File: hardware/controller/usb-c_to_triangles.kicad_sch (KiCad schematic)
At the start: 14 parts, among them J1 USB_C_Receptacle_USB2.0_16P, J2 USB_C_Receptacle_USB2.0_16P, U1 SN74LVC1T45DBV, U2 SN74LVC1T45DBV

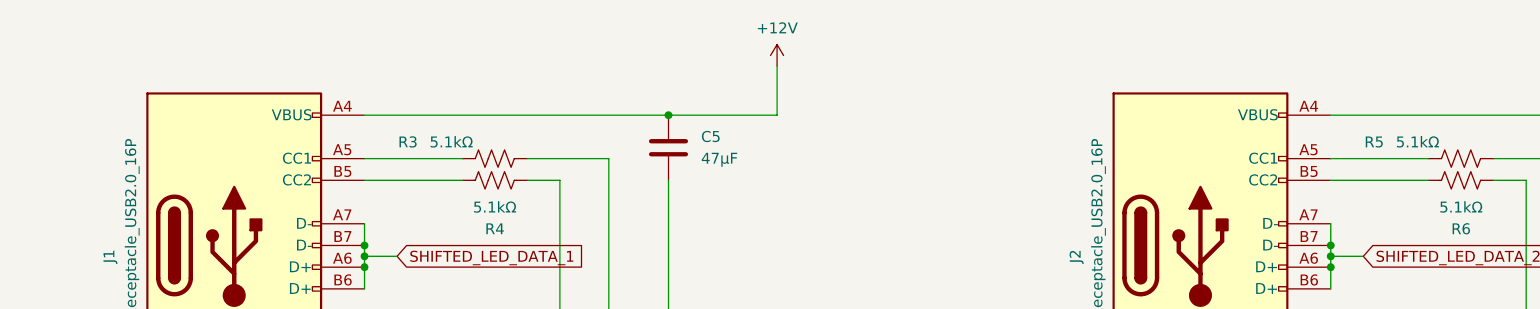
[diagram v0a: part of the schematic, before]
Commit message: adding labels and the barrel connector
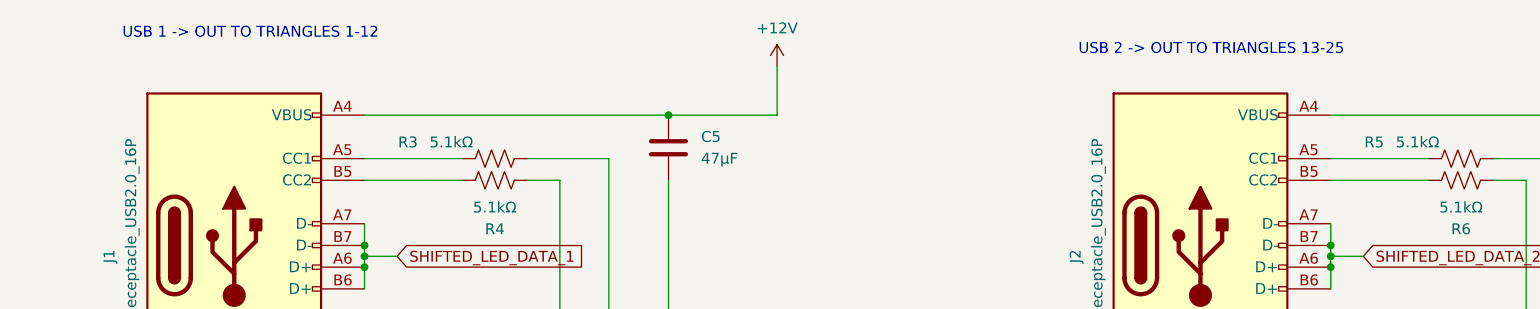
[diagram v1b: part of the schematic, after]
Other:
- note added: "USB 1 -> OUT TO TRIANGLES 1-12"
- note added: "USB 2 -> OUT TO TRIANGLES 13-25"
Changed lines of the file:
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@@
 	(generator_version "10.0")
 	(paper "A4")
+	(text "USB 2 -> OUT TO TRIANGLES 13-25"
+		(exclude_from_sim no)
+		(at 163.83 40.64 0)
+		(effects
+			(font
+				(size 1.27 1.27)
+			)
+		)
+	)
+	(text "USB 1 -> OUT TO TRIANGLES 1-12"
+		(exclude_from_sim no)
+		(at 51.435 38.735 0)
+		(effects
+			(font
+				(size 1.27 1.27)
+			)
+		)
+	)
 	(text "LEVEL SHIFTER 1"
 		(exclude_from_sim no)

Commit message: hook up all the dabao headers and one more voltage converter
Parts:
- C5, C8: footprint Capacitor_SMD:C_1206_3216Metric -> Capacitor_SMD:C_1210_3225Metric
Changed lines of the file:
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@@
 			)
 		)
-		(property "Footprint" "Capacitor_SMD:C_1206_3216Metric"
+		(property "Footprint" "Capacitor_SMD:C_1210_3225Metric"
 			(at 99.3648 48.26 0)
 			(hide yes)
@@
 			)
 		)
-		(property "Footprint" "Capacitor_SMD:C_1206_3216Metric"
+		(property "Footprint" "Capacitor_SMD:C_1210_3225Metric"
 			(at 212.3948 48.26 0)
 			(hide yes)

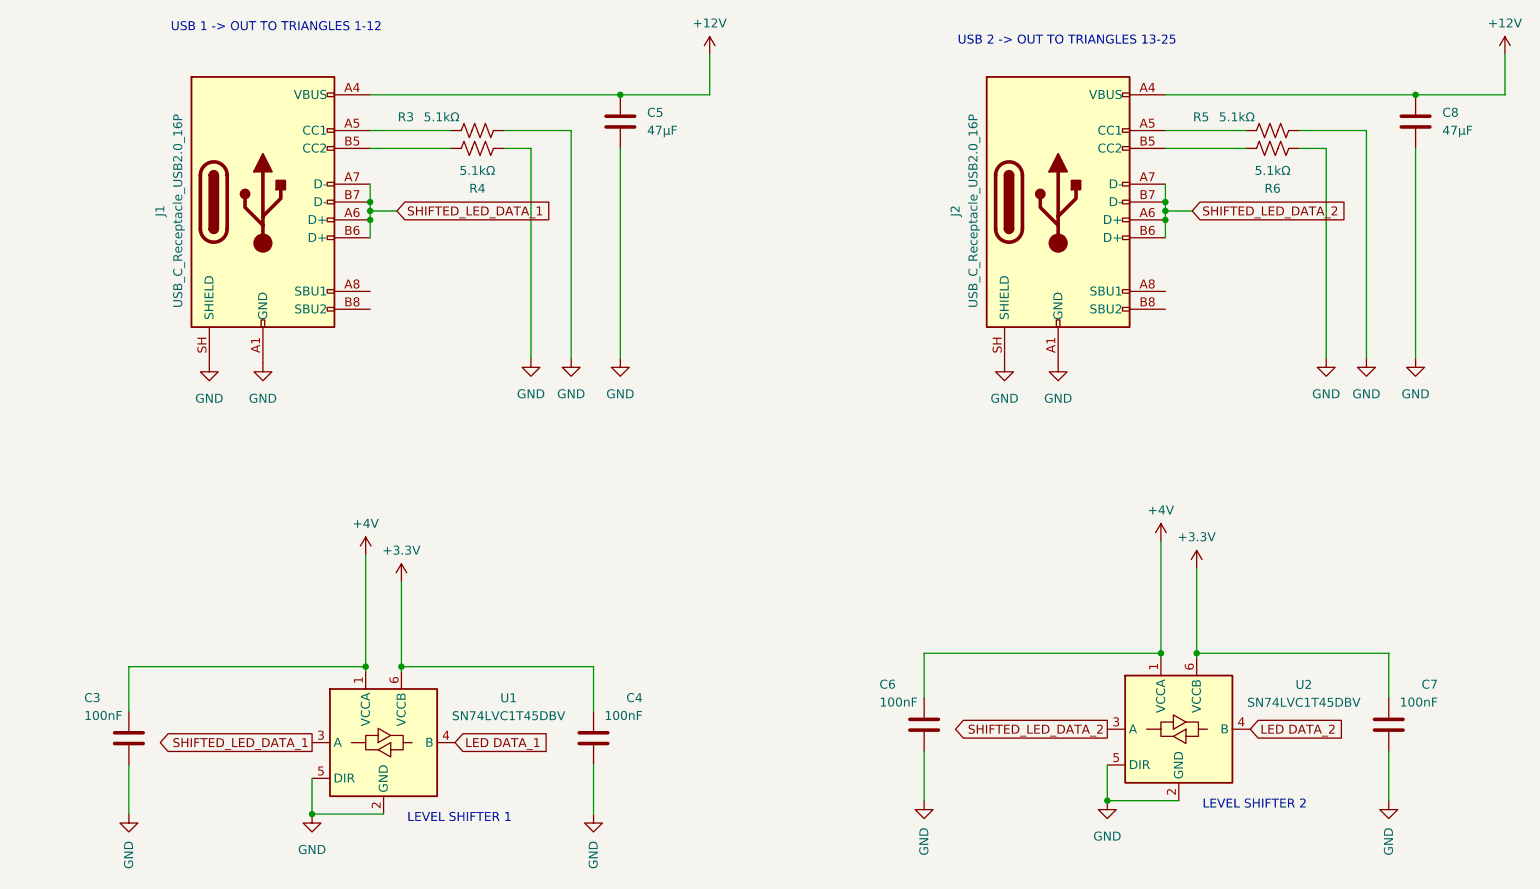
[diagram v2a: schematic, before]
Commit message: re-order the numbers on the schematic for tidiness
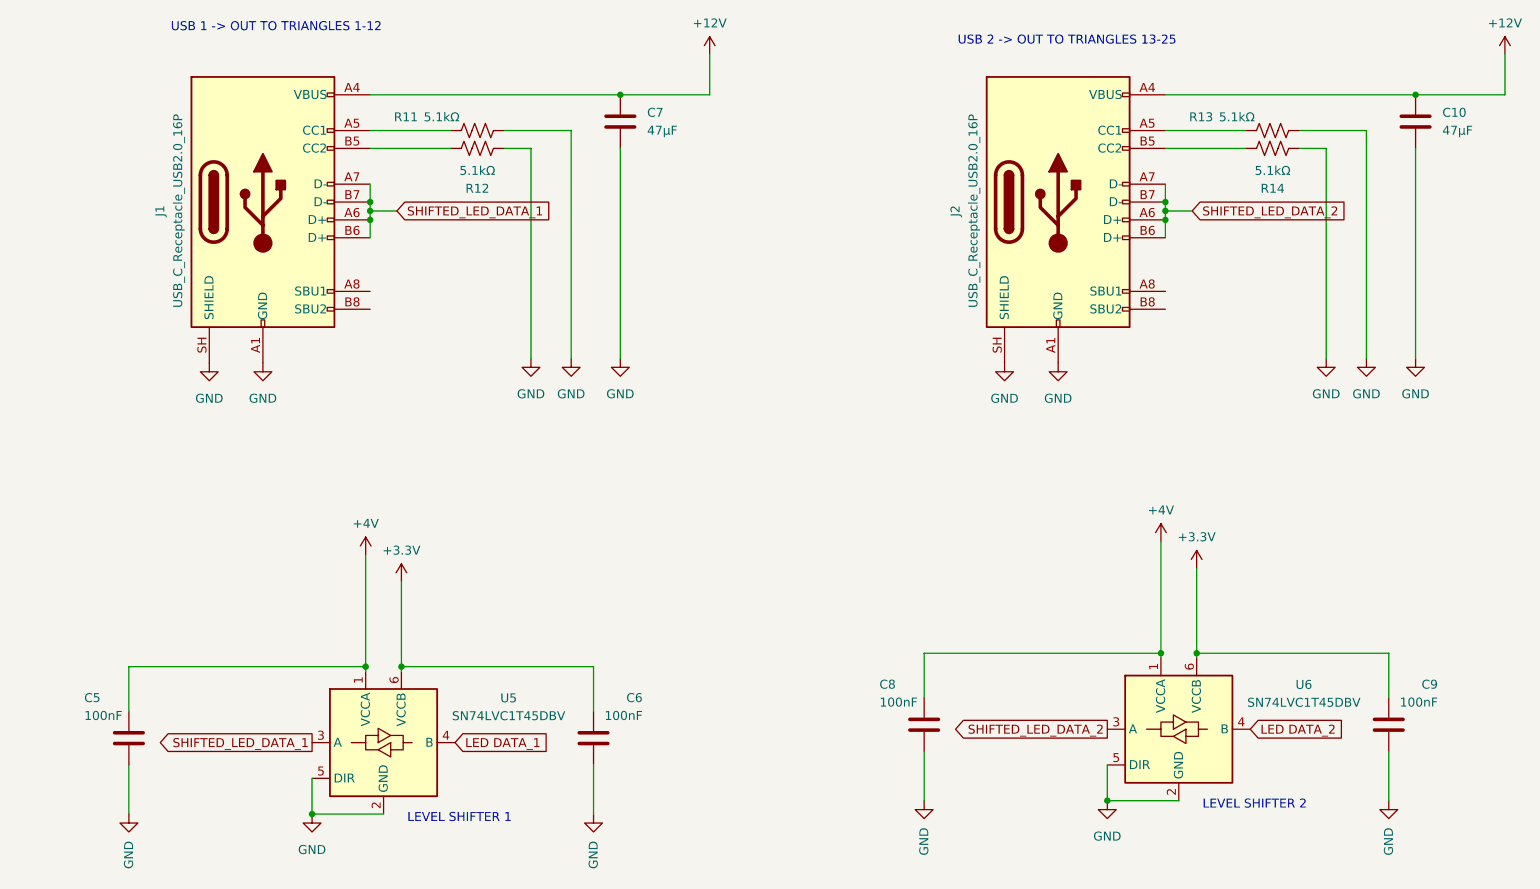
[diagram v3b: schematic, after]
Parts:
- renumbered C8 to C10, C3 to C5, C4 to C6, C5 to C7, C6 to C8, C7 to C9, R3 to R11, R4 to R12, R5 to R13, R6 to R14, U1 to U5, U2 to U6

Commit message: renaming parts for consistency
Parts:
- C10, C7: JLCPCB Part # C77101 -> (none); LCSC Part # (none) -> C77101
- C5, C6, C8, C9: JLCPCB Part # C1525 -> (none); LCSC Part # (none) -> C1525
- J1, J2: JLCPCB # C3151749 -> (none); LCSC Part # (none) -> C3151749
- R11, R12, R13, R14: JLCPCB Part # C23186 -> (none); LCSC Part # (none) -> C23186
- U5, U6: JLCPCB Part # C7843 -> (none); LCSC Part # (none) -> C7843
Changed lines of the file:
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@@
 			)
 		)
-		(property "LCSC Part Number" ""
-			(at 30.48 139.7 0)
-			(hide yes)
-			(show_name no)
-			(do_not_autoplace no)
-			(effects
-				(font
-					(size 1.27 1.27)
-				)
-			)
-		)
-		(property "JLCPCB Part #" "C1525"
+		(property "LCSC Part #" "C1525"
 			(at 30.48 139.7 0)
 			(hide yes)
@@
 			)
 		)
-		(property "JLCPCB Part #" "C23186"
+		(property "LCSC Part #" "C23186"
 			(at 193.04 55.88 90)
 			(hide yes)
@@
 			)
 		)
-		(property "LCSC Part Number" ""
-			(at 143.51 137.795 0)
-			(hide yes)
-			(show_name no)
-			(do_not_autoplace no)
-			(effects
-				(font
-					(size 1.27 1.27)
-				)
-			)
-		)
-		(property "JLCPCB Part #" "C1525"
+		(property "LCSC Part #" "C1525"
 			(at 143.51 137.795 0)
 			(hide yes)
@@
 			)
 		)
-		(property "JLCPCB Part #" "C23186"
+		(property "LCSC Part #" "C23186"
 			(at 80.01 55.88 90)
 			(hide yes)
@@
 			)
 		)
-		(property "JLCPCB Part #" "C23186"
+		(property "LCSC Part #" "C23186"
 			(at 80.01 53.34 90)
 			(hide yes)
@@
 			)
 		)
-		(property "LCSC Part Number" ""
-			(at 209.55 137.795 0)
-			(hide yes)
-			(show_name no)
-			(do_not_autoplace no)
-			(effects
-				(font
-					(size 1.27 1.27)
-				)
-			)
-		)
-		(property "JLCPCB Part #" "C1525"
+		(property "LCSC Part #" "C1525"
 			(at 209.55 137.795 0)
 			(hide yes)
@@
 			)
 		)
-		(property "JLCPCB Part #" "C7843"
+		(property "LCSC Part #" "C7843"
 			(at 66.675 140.335 0)
 			(hide yes)
@@
 			)
 		)
-		(property "JLCPCB Part #" "C77101"
+		(property "LCSC Part #" "C77101"
 			(at 100.33 52.07 0)
 			(hide yes)
@@
 			)
 		)
-		(property "LCSC Part Number" ""
-			(at 96.52 139.7 0)
-			(hide yes)
-			(show_name no)
-			(do_not_autoplace no)
-			(effects
-				(font
-					(size 1.27 1.27)
-				)
-			)
-		)
-		(property "JLCPCB Part #" "C1525"
+		(property "LCSC Part #" "C1525"
 			(at 96.52 139.7 0)
 			(hide yes)
@@
 			)
 		)
-		(property "JLCPCB Part #" "C23186"
+		(property "LCSC Part #" "C23186"
 			(at 193.04 53.34 90)
 			(hide yes)
@@
 			)
 		)
-		(property "JLCPCB #" "C3151749"
+		(property "LCSC Part #" "C3151749"
 			(at 162.56 63.5 90)
 			(hide yes)
@@
 			)
 		)
-		(property "JLCPCB Part #" "C77101"
+		(property "LCSC Part #" "C77101"
 			(at 213.36 52.07 0)
 			(hide yes)
@@
 			)
 		)
-		(property "JLCPCB Part #" "C7843"
+		(property "LCSC Part #" "C7843"
 			(at 179.705 138.43 0)
 			(hide yes)
@@
 			)
 		)
-		(property "JLCPCB #" "C3151749"
+		(property "LCSC Part #" "C3151749"
 			(at 49.53 63.5 90)
 			(hide yes)

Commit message: more footprint updating
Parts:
- J1, J2: footprint footprints:TYPE-C-SMD_USB4120-03-C -> easyeda2kicad:TYPE-C-SMD_USB4120-03-C
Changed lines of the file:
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@@
 			)
 		)
-		(property "Footprint" "footprints:TYPE-C-SMD_USB4120-03-C"
+		(property "Footprint" "easyeda2kicad:TYPE-C-SMD_USB4120-03-C"
 			(at 166.37 63.5 0)
 			(hide yes)
@@
 			)
 		)
-		(property "Footprint" "footprints:TYPE-C-SMD_USB4120-03-C"
+		(property "Footprint" "easyeda2kicad:TYPE-C-SMD_USB4120-03-C"
 			(at 53.34 63.5 0)
 			(hide yes)

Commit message: updating symbols and board
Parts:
- removed J2: USB_C_Receptacle_USB2.0_16P, easyeda2kicad:TYPE-C-SMD_USB4120-03-C, symbol Connector:USB_C_Receptacle_USB2.0_16P
- added J2: TYPE-C 16PLT-H10.0, easyeda2kicad:TYPE-C-SMD_USB4120-03-C, symbol easyeda2kicad:TYPE-C16PLT-H10.0
- J1: value USB_C_Receptacle_USB2.0_16P -> TYPE-C 16PLT-H10.0; symbol Connector:USB_C_Receptacle_USB2.0_16P -> easyeda2kicad:TYPE-C16PLT-H10.0
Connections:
- net +12V: now also J2.A4 (VBUS), J2.A9 (VBUS), J2.B4 (VBUS), J2.B9 (VBUS)
- net GND: now also J1.0 (EH), R12.2, R13.2, J2.0 (EH), J2.A1 (GND), J2.A12 (GND), J2.B1 (GND), J2.B12 (GND); no longer J1.SH (SHIELD), R12.1, R13.1
- net SHIFTED_LED_DATA_2: now also J2.A6 (DP1), J2.A7 (DN1), J2.B6 (DP2), J2.B7 (DN2)
- net at R14.2: now also J2.A5 (CC1)
- net at J1.B5 (CC2): now also R12.1; no longer R12.2
- new net: J2.B5 (CC2), R13.1
- no-connect marks 0 -> 4
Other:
- moved on the sheet: C7, R11, R12
